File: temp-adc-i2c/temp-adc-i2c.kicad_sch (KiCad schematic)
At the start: 22 parts, among them J1 Conn_01x06, U1 MCP3204

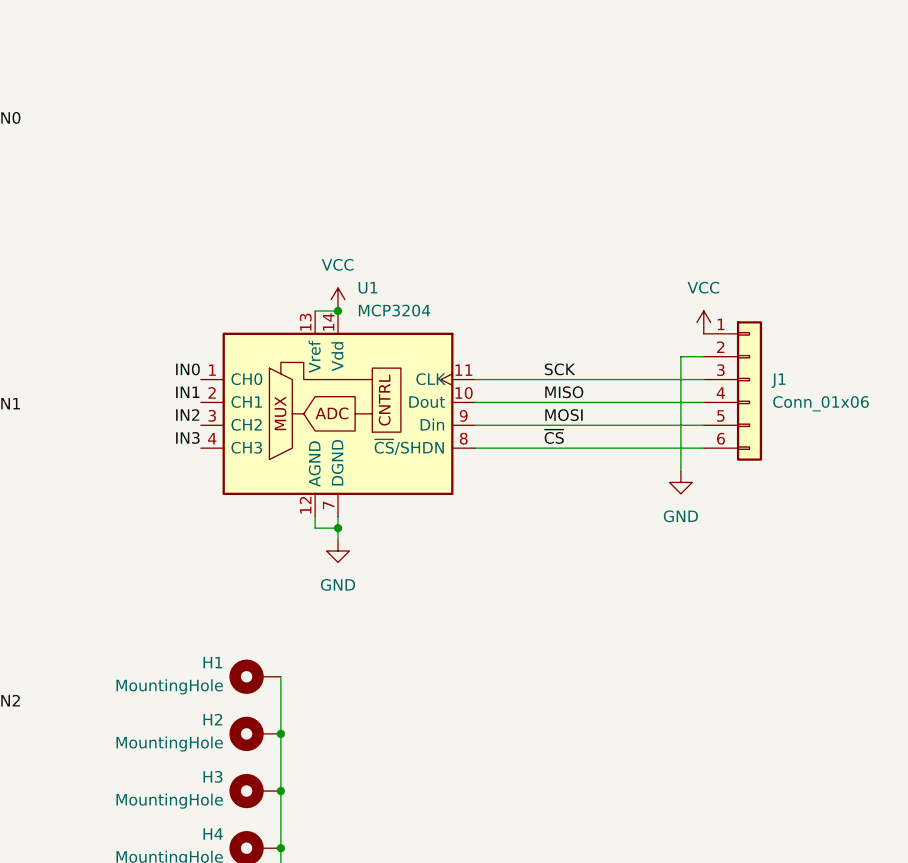
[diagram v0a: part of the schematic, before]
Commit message: Created i2c adc project and schematic
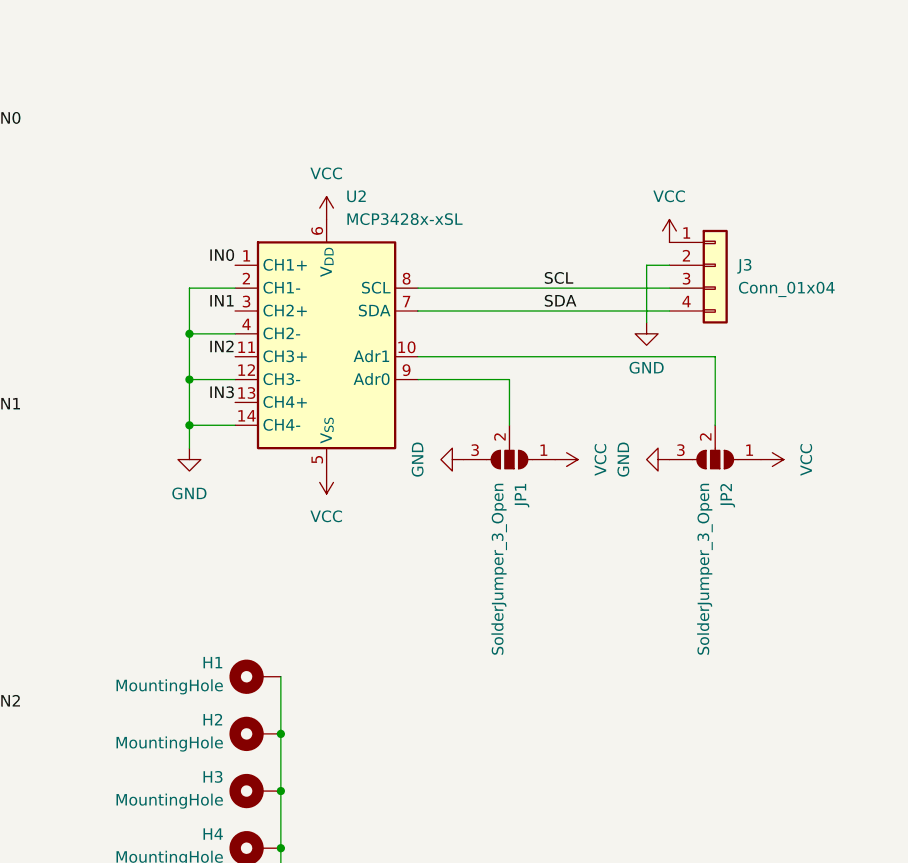
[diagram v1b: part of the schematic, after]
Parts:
- removed J1: Conn_01x06, Connector_PinHeader_2.54mm:PinHeader_1x06_P2.54mm_Vertical, symbol Connector_Generic:Conn_01x06
- removed U1: MCP3204, Package_SO:SOIC-14_3.9x8.7mm_P1.27mm, symbol Analog_ADC:MCP3204
- added J3: Conn_01x04, Connector_PinHeader_2.54mm:PinHeader_1x04_P2.54mm_Vertical, symbol Connector_Generic:Conn_01x04
- added JP1, JP2: SolderJumper_3_Open, Jumper:SolderJumper-2_P1.3mm_Open_Pad1.0x1.5mm, symbol Jumper:SolderJumper_3_Open
- added U2: MCP3428x-xSL, Package_SO:SOIC-14_3.9x8.7mm_P1.27mm, symbol Analog_ADC:MCP3428x-xSL
- H1, H2, H3, H4: footprint MountingHole:MountingHole_M2.5_thinoutline -> MountingHole:MountingHole_2.5mm
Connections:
- net GND: now also J3.2 (Pin_2), JP1.3 (B), JP2.3 (B), U2.12 (CH3-), U2.14 (CH4-), U2.2 (CH1-), U2.4 (CH2-)
- net IN0: now also U2.1 (CH1+)
- net IN1: now also U2.3 (CH2+)
- net IN2: now also U2.11 (CH3+)
- net IN3: now also U2.13 (CH4+)
- net VCC: now also J3.1 (Pin_1), JP1.1 (A), JP2.1 (A), U2.5 (V_{SS}), U2.6 (V_{DD})
- new net: JP2.2 (C), U2.10 (Adr1)
- new net: JP1.2 (C), U2.9 (Adr0)
- new net SCL: J3.3 (Pin_3), U2.8 (SCL)
- new net SDA: J3.4 (Pin_4), U2.7 (SDA)
